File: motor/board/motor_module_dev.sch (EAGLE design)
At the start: 74 parts, among them IC6 LTC6088, IC7 DRV8833RTY

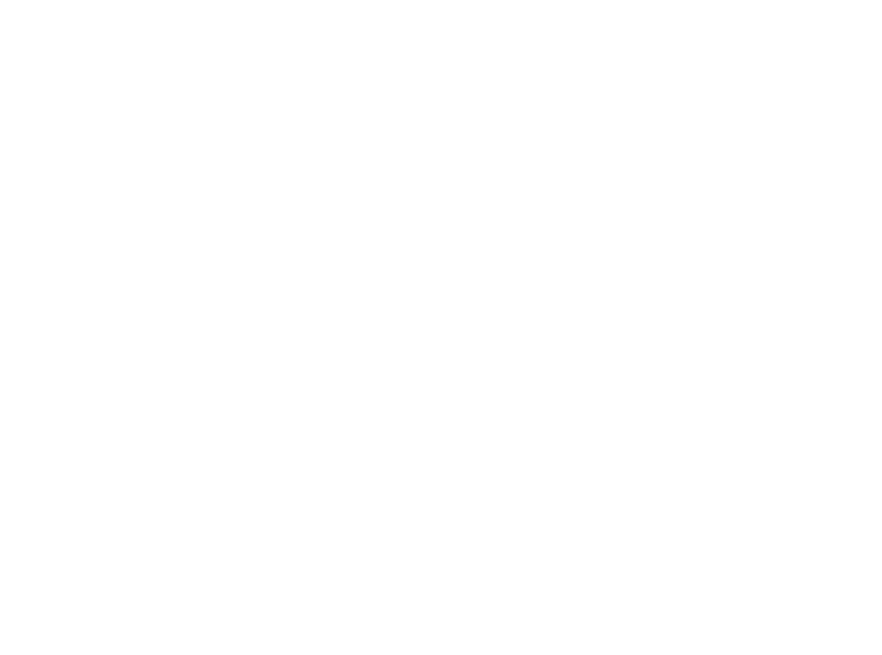
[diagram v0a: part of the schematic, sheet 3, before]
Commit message: Switched I2C and Charge pins for better Arduino compatability. Adding dev version
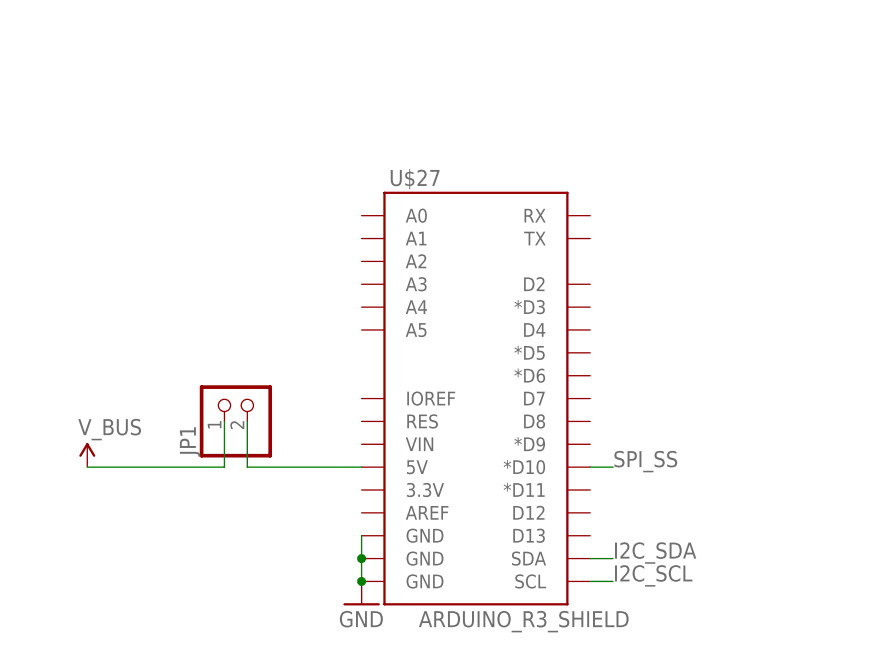
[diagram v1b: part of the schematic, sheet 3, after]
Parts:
- added JP1: (no value), pinhead:PINHD-1X2
- added U$27: ARDUINO_R3_SHIELD, SparkFun-Boards:ARDUINO_R3_SHIELD
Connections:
- new net N$10: JP1.2, U$27.5V
- net GND: now also U$27.GND@0, U$27.GND@1, U$27.GND@2
- net I2C_SCL: now also U$27.SCL
- net I2C_SDA: now also U$27.SDA
- net SPI_SS: now also U$27.*D10
- net V_BUS: now also JP1.1
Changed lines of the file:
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@@
 <part name="GND14" library="supply1" deviceset="GND" device=""/>
 <part name="U$16" library="modular_robotics" deviceset="V_3.0" device=""/>
+<part name="U$27" library="SparkFun-Boards" deviceset="ARDUINO_R3_SHIELD" device=""/>
+<part name="GND15" library="supply1" deviceset="GND" device=""/>
+<part name="JP1" library="pinhead" deviceset="PINHD-1X2" device=""/>
+<part name="U$28" library="modular_robotics" deviceset="V_BUS" device=""/>
 </parts>
 <sheets>
@@
 <instance part="R37" gate="G$1" x="114.3" y="149.86" rot="R90"/>
 <instance part="R38" gate="G$1" x="106.68" y="149.86" rot="R90"/>
+<instance part="U$27" gate="G$1" x="60.96" y="53.34"/>
+<instance part="GND15" gate="1" x="48.26" y="27.94"/>
+<instance part="JP1" gate="G$1" x="35.56" y="50.8" rot="R90"/>
+<instance part="U$28" gate="G$1" x="17.78" y="43.18"/>
 </instances>
 <busses>
@@
 <junction x="175.26" y="127"/>
 </segment>
+<segment>
+<pinref part="U$27" gate="G$1" pin="GND@2"/>
+<pinref part="U$27" gate="G$1" pin="GND@1"/>
+<wire x1="48.26" y1="35.56" x2="48.26" y2="33.02" width="0.1524" layer="91"/>
+<pinref part="U$27" gate="G$1" pin="GND@0"/>
+<wire x1="48.26" y1="33.02" x2="48.26" y2="30.48" width="0.1524" layer="91"/>
+<junction x="48.26" y="33.02"/>
+<pinref part="GND15" gate="1" pin="GND"/>
+<junction x="48.26" y="30.48"/>
+</segment>
 </net>
 <net name="SWD_CLK" class="0">
@@
 <label x="60.96" y="119.38" size="1.778" layer="95"/>
 </segment>
+<segment>
+<pinref part="U$27" gate="G$1" pin="SCL"/>
+<wire x1="73.66" y1="30.48" x2="76.2" y2="30.48" width="0.1524" layer="91"/>
+<label x="76.2" y="30.48" size="1.778" layer="95"/>
+</segment>
 </net>
 <net name="I2C_SDA" class="0">
@@
 <label x="60.96" y="116.84" size="1.778" layer="95"/>
 </segment>
+<segment>
+<pinref part="U$27" gate="G$1" pin="SDA"/>
+<wire x1="73.66" y1="33.02" x2="76.2" y2="33.02" width="0.1524" layer="91"/>
+<label x="76.2" y="33.02" size="1.778" layer="95"/>
+</segment>
 </net>
 <net name="SPI_SS" class="0">
@@
 <label x="215.9" y="149.86" size="1.778" layer="95"/>
 </segment>
+<segment>
+<pinref part="U$27" gate="G$1" pin="*D10"/>
+<wire x1="73.66" y1="43.18" x2="76.2" y2="43.18" width="0.1524" layer="91"/>
+<label x="76.2" y="43.18" size="1.778" layer="95"/>
+</segment>
 </net>
 <net name="SPI_MISO" class="0">
@@
 </segment>
 </net>
+<net name="N$10" class="0">
+<segment>
+<pinref part="U$27" gate="G$1" pin="5V"/>
+<pinref part="JP1" gate="G$1" pin="2"/>
+<wire x1="48.26" y1="43.18" x2="35.56" y2="43.18" width="0.1524" layer="91"/>
+<wire x1="35.56" y1="43.18" x2="35.56" y2="48.26" width="0.1524" layer="91"/>
+</segment>
+</net>
+<net name="V_BUS" class="0">
+<segment>
+<pinref part="JP1" gate="G$1" pin="1"/>
+<wire x1="33.02" y1="48.26" x2="33.02" y2="43.18" width="0.1524" layer="91"/>
+<wire x1="33.02" y1="43.18" x2="17.78" y2="43.18" width="0.1524" layer="91"/>
+<pinref part="U$28" gate="G$1" pin="V_BUS"/>
+</segment>
+</net>

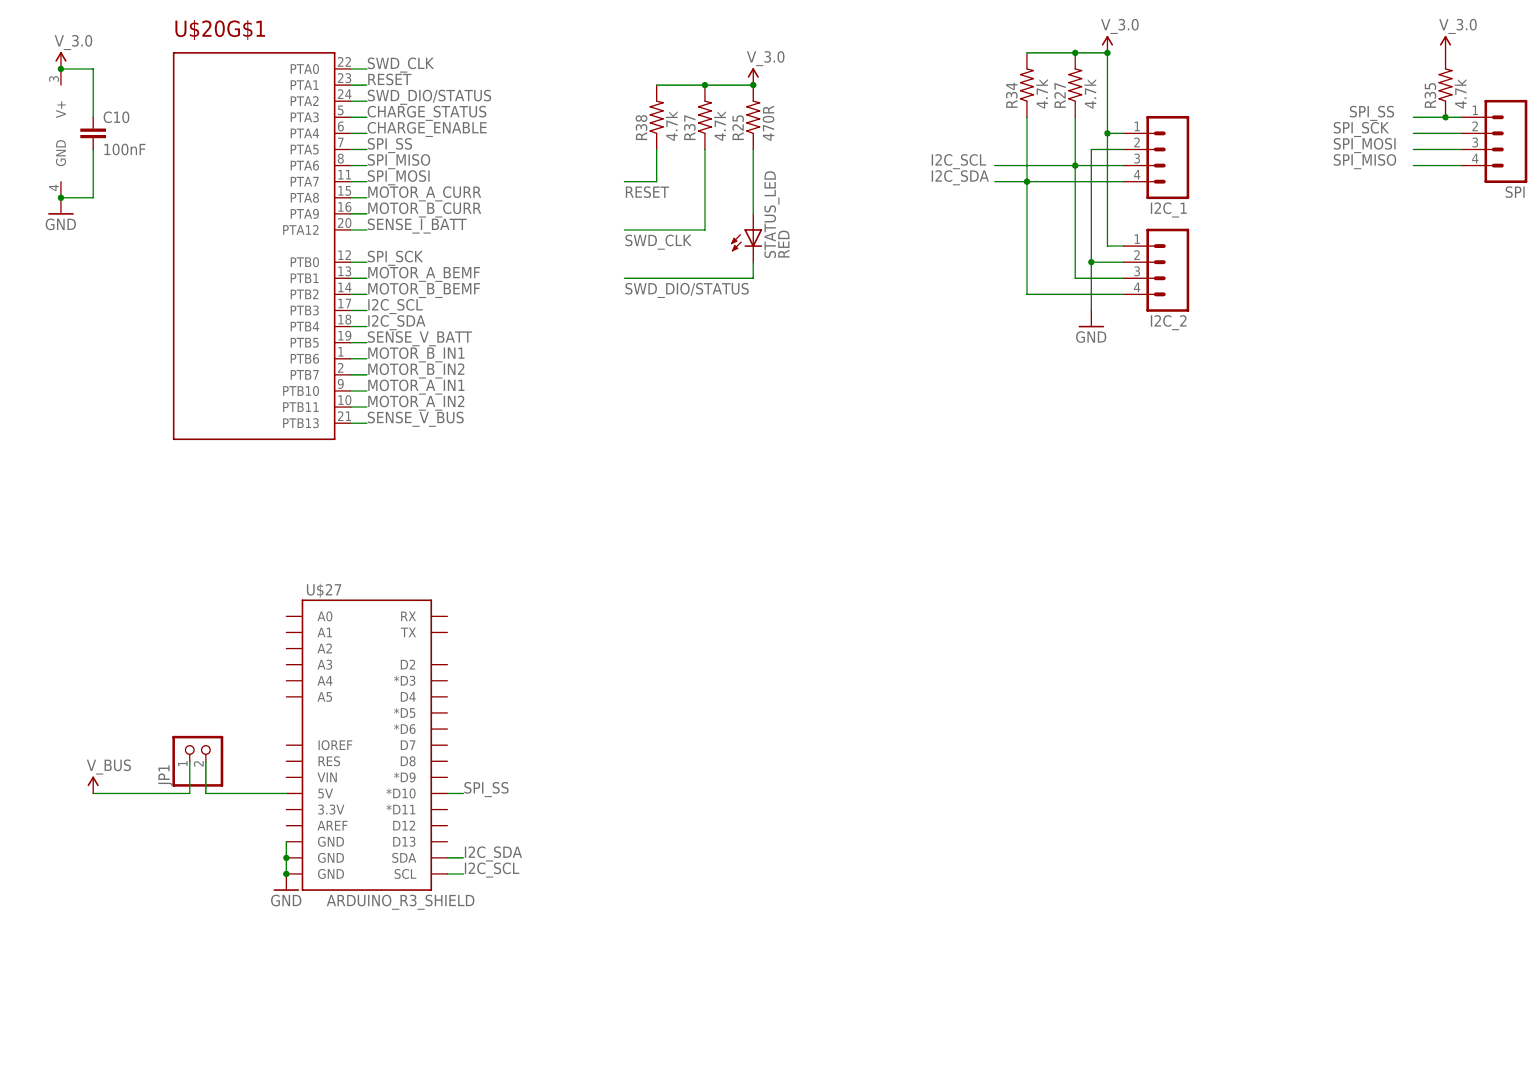
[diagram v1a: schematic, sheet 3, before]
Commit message: Added parallel pull-up to status
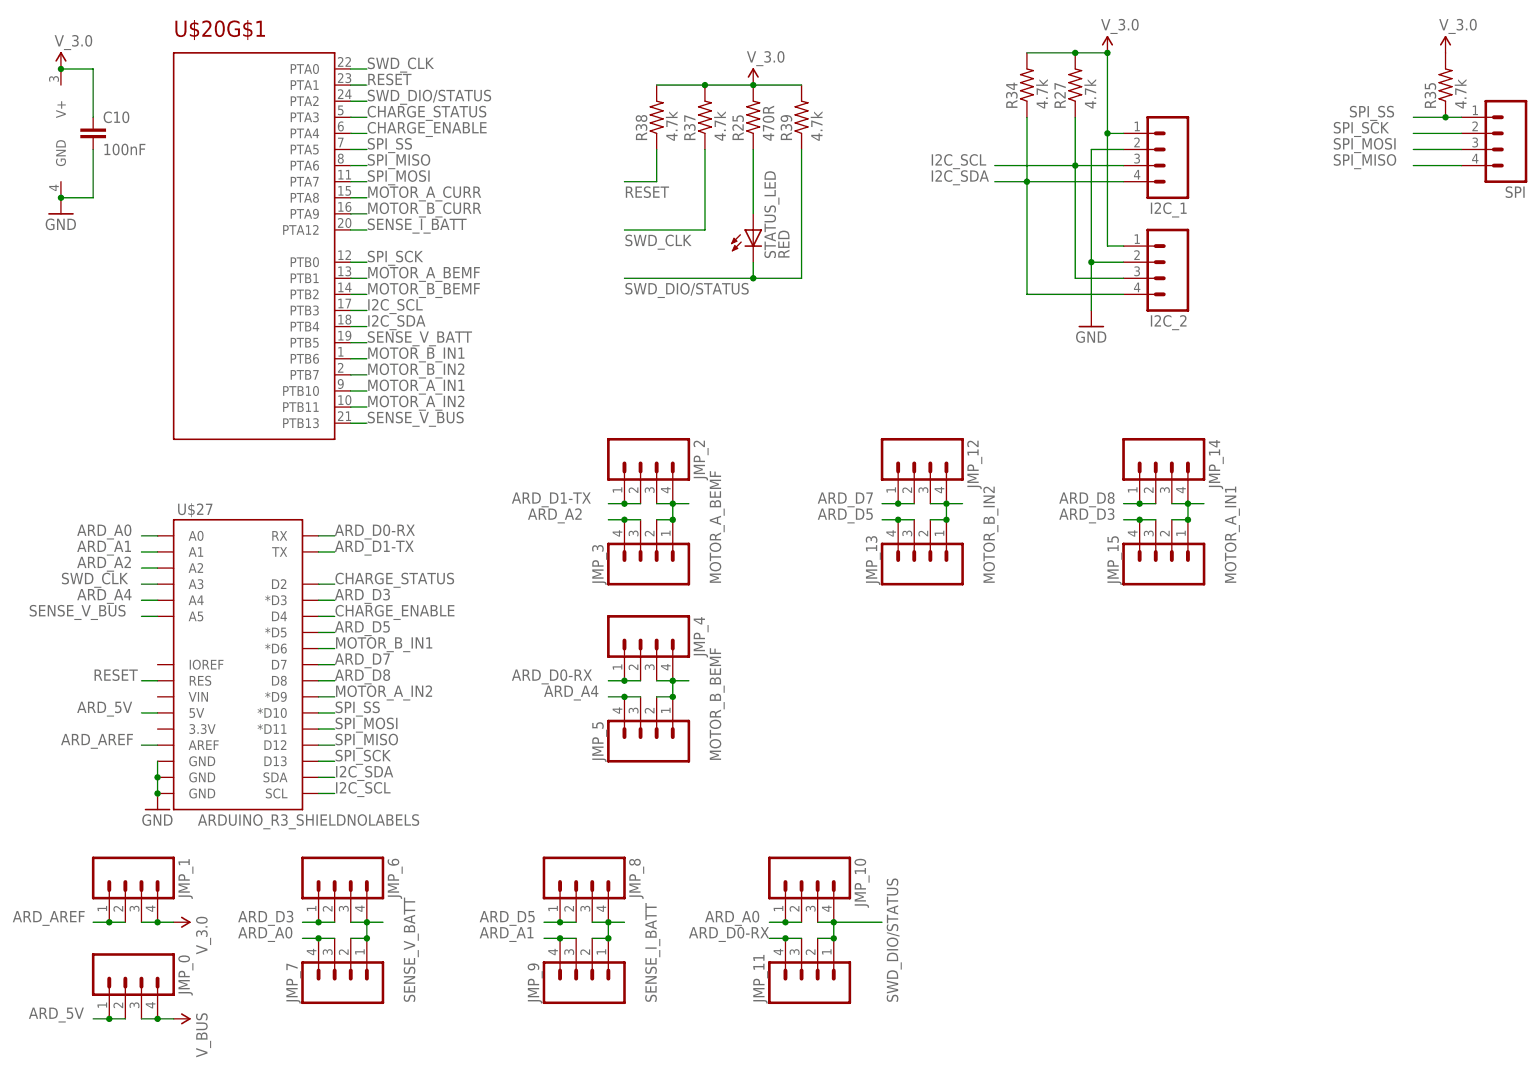
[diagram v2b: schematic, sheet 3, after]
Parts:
- removed JP1: (no value), pinhead:PINHD-1X2
- added JMP_0, JMP_1, JMP_10, JMP_11, JMP_12, JMP_13, JMP_14, JMP_15, JMP_2, JMP_3, JMP_4, JMP_5, JMP_6, JMP_7, JMP_8, JMP_9: (no value), modular_robotics:M041X04_NO_SILK
- added R39: 4.7k, biomimetic:RESISTOR0402-RES
- SPI: device modular_robotics:M04FFC -> modular_robotics:M041X04_NO_SILK
- U$27: value ARDUINO_R3_SHIELD -> ARDUINO_R3_SHIELDNOLABELS; device SparkFun-Boards:ARDUINO_R3_SHIELD -> SparkFun-Boards:ARDUINO_R3_SHIELDNOLABELS
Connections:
- removed net N$10: JP1.2, U$27.5V
- new net ARD_5V: JMP_0.1, JMP_0.2, U$27.5V
- new net ARD_A0: JMP_10.1, JMP_10.2, JMP_7.3, JMP_7.4, U$27.A0
- new net ARD_A1: JMP_9.3, JMP_9.4, U$27.A1
- new net ARD_A2: JMP_3.3, JMP_3.4, U$27.A2
- new net ARD_A4: JMP_5.3, JMP_5.4, U$27.A4
- new net ARD_AREF: JMP_1.1, JMP_1.2, U$27.AREF
- new net ARD_D0-RX: JMP_11.3, JMP_11.4, JMP_4.1, JMP_4.2, U$27.RX
- new net ARD_D1-TX: JMP_2.1, JMP_2.2, U$27.TX
- new net ARD_D3: JMP_15.3, JMP_15.4, JMP_6.1, JMP_6.2, U$27.*D3
- new net ARD_D5: JMP_13.3, JMP_13.4, JMP_8.1, JMP_8.2, U$27.*D5
- new net ARD_D7: JMP_12.1, JMP_12.2, U$27.D7
- new net ARD_D8: JMP_14.1, JMP_14.2, U$27.D8
- net CHARGE_ENABLE: now also U$27.D4
- net CHARGE_STATUS: now also U$27.D2
- net MOTOR_A_BEMF: now also JMP_2.3, JMP_2.4, JMP_3.1, JMP_3.2
- net MOTOR_A_IN1: now also JMP_14.3, JMP_14.4, JMP_15.1, JMP_15.2
- net MOTOR_A_IN2: now also U$27.*D9
- net MOTOR_B_BEMF: now also JMP_4.3, JMP_4.4, JMP_5.1, JMP_5.2
- net MOTOR_B_IN1: now also U$27.*D6
- net MOTOR_B_IN2: now also JMP_12.3, JMP_12.4, JMP_13.1, JMP_13.2
- net RESET: now also U$27.RES
- net SENSE_I_BATT: now also JMP_8.3, JMP_8.4, JMP_9.1, JMP_9.2
- net SENSE_V_BATT: now also JMP_6.3, JMP_6.4, JMP_7.1, JMP_7.2
- net SENSE_V_BUS: now also U$27.A5
- net SPI_MISO: now also U$27.D12
- net SPI_MOSI: now also U$27.*D11
- net SPI_SCK: now also U$27.D13
- net SWD_CLK: now also U$27.A3
- net SWD_DIO/STATUS: now also JMP_10.3, JMP_10.4, JMP_11.1, JMP_11.2, R39.1
- net V_3.0: now also JMP_1.3, JMP_1.4, R39.2
- net V_BUS: now also JMP_0.3, JMP_0.4; no longer JP1.1
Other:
- moved on the sheet: U$27

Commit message: Layout complete. Need to fix some crossing wires, tidy up, figure out if need to fix A4/A2 connection issue.
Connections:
- net MOTOR_A_ISEN: now also IC6A.+IN; no longer IC6B.+IN
- net MOTOR_B_ISEN: now also IC6B.+IN; no longer IC6C.+IN
- net N$22: now also IC6C.-IN; no longer IC6D.-IN
- net N$23: now also IC6C.+IN; no longer IC6D.+IN
- net N$24: now also IC6A.-IN; no longer IC6B.-IN
- net N$26: now also IC6B.-IN; no longer IC6C.-IN
- net N$30: now also IC6D.-IN; no longer IC6A.-IN
- net N$31: now also IC6D.+IN; no longer IC6A.+IN
- net N$34: now also IC6B.OUT; no longer IC6C.OUT
- net N$35: now also IC6A.OUT; no longer IC6B.OUT
- net N$36: now also IC6D.OUT; no longer IC6A.OUT
- net N$37: now also IC6C.OUT; no longer IC6D.OUT
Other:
- moved on the sheet: IC6A, IC6B, IC6C, IC6D
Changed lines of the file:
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@@
 </instance>
 <instance part="FRAME3" gate="G$2" x="147.32" y="0"/>
-<instance part="IC6" gate="A" x="154.94" y="167.64" rot="MR180"/>
-<instance part="IC6" gate="D" x="154.94" y="132.08" rot="MR180"/>
-<instance part="IC6" gate="B" x="154.94" y="93.98" rot="MR180"/>
-<instance part="IC6" gate="C" x="154.94" y="58.42" rot="MR180"/>
+<instance part="IC6" gate="D" x="154.94" y="167.64" rot="MR180"/>
+<instance part="IC6" gate="C" x="154.94" y="132.08" rot="MR180"/>
+<instance part="IC6" gate="A" x="154.94" y="93.98" rot="MR180"/>
+<instance part="IC6" gate="B" x="154.94" y="58.42" rot="MR180"/>
 <instance part="IC6" gate="P" x="226.06" y="165.1" smashed="yes">
 <attribute name="NAME" x="218.44" y="173.99" size="1.778" layer="95"/>
@@
 <pinref part="R14" gate="G$1" pin="1"/>
 <wire x1="147.32" y1="177.8" x2="152.4" y2="177.8" width="0.1524" layer="91"/>
-<pinref part="IC6" gate="A" pin="-IN"/>
+<pinref part="IC6" gate="D" pin="-IN"/>
 <wire x1="149.86" y1="170.18" x2="147.32" y2="170.18" width="0.1524" layer="91"/>
 <junction x="147.32" y="170.18"/>
@@
 <pinref part="R15" gate="G$1" pin="2"/>
 <wire x1="147.32" y1="165.1" x2="147.32" y2="162.56" width="0.1524" layer="91"/>
-<pinref part="IC6" gate="A" pin="+IN"/>
+<pinref part="IC6" gate="D" pin="+IN"/>
 <wire x1="149.86" y1="165.1" x2="147.32" y2="165.1" width="0.1524" layer="91"/>
 <junction x="147.32" y="165.1"/>
@@
 <pinref part="R18" gate="G$1" pin="1"/>
 <wire x1="147.32" y1="142.24" x2="152.4" y2="142.24" width="0.1524" layer="91"/>
-<pinref part="IC6" gate="D" pin="-IN"/>
+<pinref part="IC6" gate="C" pin="-IN"/>
 <wire x1="149.86" y1="134.62" x2="147.32" y2="134.62" width="0.1524" layer="91"/>
 <junction x="147.32" y="134.62"/>
@@
 <pinref part="R19" gate="G$1" pin="2"/>
 <wire x1="147.32" y1="129.54" x2="147.32" y2="127" width="0.1524" layer="91"/>
-<pinref part="IC6" gate="D" pin="+IN"/>
+<pinref part="IC6" gate="C" pin="+IN"/>
 <wire x1="149.86" y1="129.54" x2="147.32" y2="129.54" width="0.1524" layer="91"/>
 <junction x="147.32" y="129.54"/>
@@
 <pinref part="R22" gate="G$1" pin="1"/>
 <wire x1="147.32" y1="104.14" x2="152.4" y2="104.14" width="0.1524" layer="91"/>
-<pinref part="IC6" gate="B" pin="-IN"/>
+<pinref part="IC6" gate="A" pin="-IN"/>
 <wire x1="149.86" y1="96.52" x2="147.32" y2="96.52" width="0.1524" layer="91"/>
 <junction x="147.32" y="96.52"/>
@@
 <pinref part="R26" gate="G$1" pin="1"/>
 <wire x1="147.32" y1="68.58" x2="152.4" y2="68.58" width="0.1524" layer="91"/>
-<pinref part="IC6" gate="C" pin="-IN"/>
+<pinref part="IC6" gate="B" pin="-IN"/>
 <wire x1="149.86" y1="60.96" x2="147.32" y2="60.96" width="0.1524" layer="91"/>
 <junction x="147.32" y="60.96"/>
@@
 <segment>
 <pinref part="R33" gate="G$1" pin="1"/>
-<pinref part="IC6" gate="C" pin="OUT"/>
+<pinref part="IC6" gate="B" pin="OUT"/>
 <wire x1="162.56" y1="58.42" x2="165.1" y2="58.42" width="0.1524" layer="91"/>
 <pinref part="R26" gate="G$1" pin="2"/>
@@
 <net name="N$35" class="0">
 <segment>
-<pinref part="IC6" gate="B" pin="OUT"/>
+<pinref part="IC6" gate="A" pin="OUT"/>
 <wire x1="162.56" y1="93.98" x2="165.1" y2="93.98" width="0.1524" layer="91"/>
 <pinref part="R22" gate="G$1" pin="2"/>
@@
 <net name="N$37" class="0">
 <segment>
-<pinref part="IC6" gate="D" pin="OUT"/>
+<pinref part="IC6" gate="C" pin="OUT"/>
 <pinref part="R31" gate="G$1" pin="1"/>
 <wire x1="162.56" y1="132.08" x2="165.1" y2="132.08" width="0.1524" layer="91"/>
@@
 <net name="N$36" class="0">
 <segment>
-<pinref part="IC6" gate="A" pin="OUT"/>
+<pinref part="IC6" gate="D" pin="OUT"/>
 <pinref part="R30" gate="G$1" pin="1"/>
 <wire x1="162.56" y1="167.64" x2="165.1" y2="167.64" width="0.1524" layer="91"/>
@@
 </segment>
 <segment>
-<pinref part="IC6" gate="B" pin="+IN"/>
+<pinref part="IC6" gate="A" pin="+IN"/>
 <wire x1="149.86" y1="91.44" x2="132.08" y2="91.44" width="0.1524" layer="91"/>
 <label x="111.76" y="91.44" size="1.778" layer="95"/>
@@
 </segment>
 <segment>
-<pinref part="IC6" gate="C" pin="+IN"/>
+<pinref part="IC6" gate="B" pin="+IN"/>
 <wire x1="149.86" y1="55.88" x2="132.08" y2="55.88" width="0.1524" layer="91"/>
 <label x="111.76" y="55.88" size="1.778" layer="95"/>

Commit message: Finished layout, round 2
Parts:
- removed I2C_1, I2C_2: (no value), modular_robotics:M04
- added JMP_16, JMP_17: (no value), modular_robotics:M041X04_NO_SILK
- added R40, R41: 470R, biomimetic:RESISTOR0402-RES
- added R42: 480R, biomimetic:RESISTOR0402-RES
- added U$30: MOTOR_HOUSING, modular_robotics:MOTOR_HOUSING
- PWR_BATT: value JST-RCY-FEMALE -> JST-RCY-FEMALEBATTERY; device modular_robotics:JST-RCY-FEMALE -> modular_robotics:JST-RCY-FEMALEBATTERY
- PWR_BUS: value JST-RCY-FEMALE -> JST-RCY-FEMALE-RA; device modular_robotics:JST-RCY-FEMALE -> modular_robotics:JST-RCY-FEMALE-RA
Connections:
- new net N$10: R41.1, SPI.3
- new net N$11: R42.1, SPI.4
- new net N$9: R40.1, SPI.2
- net ARD_A2: now also JMP_16.3, JMP_16.4
- net ARD_A4: now also JMP_17.3, JMP_17.4
- net GND: now also U$30LEFT.2, U$30RIGHT.2; no longer I2C_1.2, I2C_2.2
- net I2C_SCL: now also U$30LEFT.3, U$30RIGHT.3; no longer I2C_1.3, I2C_2.3
- net I2C_SDA: now also U$30LEFT.4, U$30RIGHT.4; no longer I2C_1.4, I2C_2.4
- net MOTOR_A_CURR: now also JMP_16.1, JMP_16.2
- net MOTOR_B_CURR: now also JMP_17.1, JMP_17.2
- net SPI_MISO: now also R42.2; no longer SPI.4
- net SPI_MOSI: now also R41.2; no longer SPI.3
- net SPI_SCK: now also R40.2; no longer SPI.2
- net V_3.0: now also U$30LEFT.1, U$30RIGHT.1; no longer I2C_1.1, I2C_2.1
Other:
- moved on the sheet: JMP_10, JMP_11, JMP_12, JMP_13, JMP_14, JMP_15, JMP_4, JMP_5, JMP_8, JMP_9
